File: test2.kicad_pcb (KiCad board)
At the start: 2 copper layers, 5 parts, among them Q1 IRLZ34N, U1 TEENSY3.1, U2 HCPL3120

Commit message: POC traco
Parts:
- added U3: TRACO_TEL_DCDC, DIP-24__600_ELL, F.Cu at (111.8, 88.9)
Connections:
- U1 pad 15: (no net) -> N-000009

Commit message: switched to version 4 of kicad...
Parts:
- Q1: footprint TO220 -> TO_SOT_Packages_THT:TO-220_Vertical
- R1: footprint R4 -> Resistors_THT:R_Axial_DIN0204_L3.6mm_D1.6mm_P5.08mm_Horizontal
- R2: footprint R3-LARGE_PADS -> Resistors_THT:R_Axial_DIN0204_L3.6mm_D1.6mm_P5.08mm_Horizontal
- U1: footprint DIP-28__600 -> Teensy:Teensy30_31_32_LC
- U2: footprint DIP-8__300 -> Housings_DIP:DIP-8_W7.62mm
- U3: footprint DIP-24__600_ELL -> Housings_DIP:DIP-24_W15.24mm
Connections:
- U1 pad 1: N-000008 -> Net-(U1-Pad1)
- U1 pad 10: (no net) -> Net-(U1-Pad10)
- U1 pad 11: (no net) -> Net-(U1-Pad11)
- U1 pad 12: (no net) -> Net-(U1-Pad12)
- U1 pad 13: (no net) -> Net-(U1-Pad13)
- U1 pad 14: (no net) -> Net-(U1-Pad14)
- U1 pad 15: N-000009 -> Net-(U1-Pad15)
- U1 pad 16: (no net) -> Net-(U1-Pad16)
- U1 pad 17: (no net) -> Net-(U1-Pad17)
- U1 pad 18: (no net) -> Net-(U1-Pad18)
- U1 pad 19: (no net) -> Net-(U1-Pad19)
- U1 pad 2: (no net) -> Net-(U1-Pad2)
- U1 pad 20: (no net) -> Net-(U1-Pad20)
- U1 pad 21: (no net) -> Net-(U1-Pad21)
- U1 pad 22: (no net) -> Net-(U1-Pad22)
- U1 pad 23: (no net) -> Net-(U1-Pad23)
- U1 pad 24: (no net) -> Net-(U1-Pad24)
- U1 pad 25: (no net) -> Net-(U1-Pad25)
- U1 pad 26: (no net) -> Net-(U1-Pad26)
- U1 pad 27: (no net) -> Net-(U1-Pad27)
- U1 pad 28: (no net) -> Net-(U1-Pad28)
- U1 pad 3: (no net) -> Net-(U1-Pad3)
- U1 pad 4: (no net) -> Net-(U1-Pad4)
- U1 pad 6: (no net) -> Net-(U1-Pad6)
- U1 pad 7: (no net) -> Net-(U1-Pad7)
- U1 pad 8: (no net) -> Net-(U1-Pad8)
- U1 pad 9: (no net) -> Net-(U1-Pad9)
- U2 pad 1: (no net) -> Net-(U2-Pad1)
- U2 pad 3: N-000008 -> Net-(U1-Pad1)
- U2 pad 4: (no net) -> Net-(U2-Pad4)
- U2 pad 6: (no net) -> Net-(U2-Pad6)
- U3 pad 1: (no net) -> Net-(U1-Pad15)
- U3 pad 10: (no net) -> +5V
- U3 pad 11: (no net) -> GND
- U3 pad 2: (no net) -> Net-(U1-Pad1)
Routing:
- net (no net): track 0.00 -> 182.4 mm
- net +5V: track 106.6 -> 0.00 mm
- net Net-(U1-Pad1): track 0.00 -> 59.7 mm
- net N-000008: track 59.7 -> 0.00 mm
- net Net-(Q1-Pad2): track 54.5 -> 0.00 mm
- net Net-(U1-Pad20): track 0.00 -> 44.3 mm
- net GND: track 38.9 -> 0.00 mm
- net Net-(Q1-Pad1): track 21.4 -> 38.9 mm

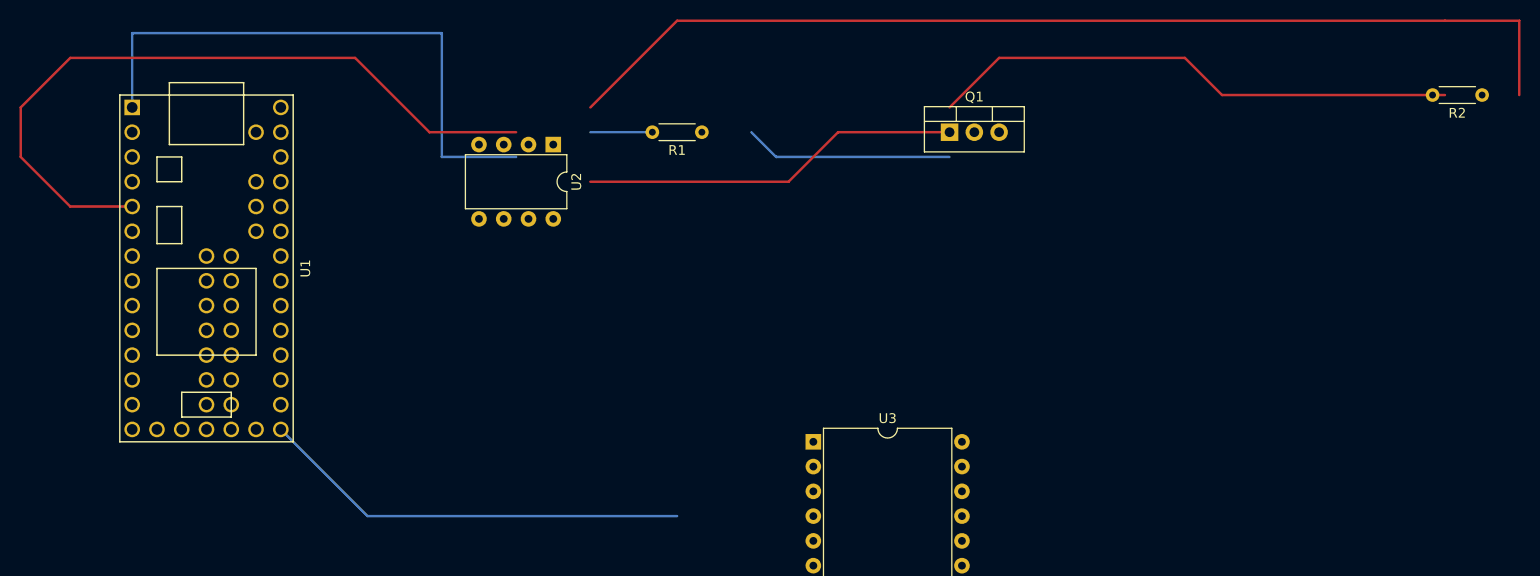
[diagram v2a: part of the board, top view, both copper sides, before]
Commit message: more messing araound to get kicad 4 happy
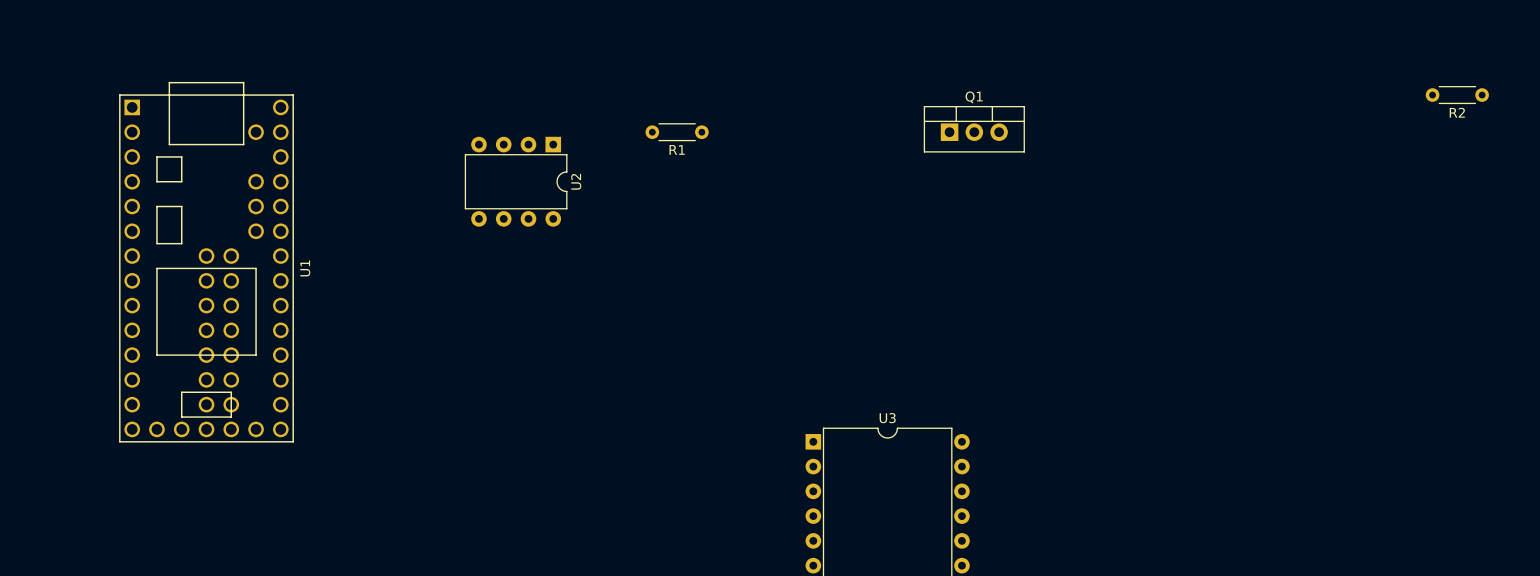
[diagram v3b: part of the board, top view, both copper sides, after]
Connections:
- U3 pad 1: Net-(U1-Pad15) -> +5V
- U3 pad 10: +5V -> Net-(U1-Pad33)
- U3 pad 11: GND -> Net-(U1-Pad1)
- U3 pad 12: (no net) -> GND
- U3 pad 2: Net-(U1-Pad1) -> (no net)
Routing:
- net (no net): track 182.4 -> 0.00 mm
- net Net-(U1-Pad5): track 74.7 -> 0.00 mm
- net Net-(U1-Pad1): track 59.7 -> 0.00 mm
- net Net-(U1-Pad20): track 44.3 -> 0.00 mm
- net Net-(Q1-Pad1): track 38.9 -> 0.00 mm
- net Net-(R1-Pad2): track 6.35 -> 0.00 mm
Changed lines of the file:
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@@
     (thickness 1.6)
     (drawings 0)
-    (tracks 27)
+    (tracks 0)
     (zones 0)
     (modules 6)
@@
     (fp_arc (start 7.62 -1.39) (end 6.62 -1.39) (angle -180) (layer F.SilkS) (width 0.12))
     (pad 1 thru_hole rect (at 0 0) (size 1.6 1.6) (drill 0.8) (layers *.Cu *.Mask)
-      (net 20 "Net-(U1-Pad15)"))
+      (net 1 +5V))
     (pad 13 thru_hole oval (at 15.24 27.94) (size 1.6 1.6) (drill 0.8) (layers *.Cu *.Mask))
-    (pad 2 thru_hole oval (at 0 2.54) (size 1.6 1.6) (drill 0.8) (layers *.Cu *.Mask)
-      (net 6 "Net-(U1-Pad1)"))
+    (pad 2 thru_hole oval (at 0 2.54) (size 1.6 1.6) (drill 0.8) (layers *.Cu *.Mask))
     (pad 14 thru_hole oval (at 15.24 25.4) (size 1.6 1.6) (drill 0.8) (layers *.Cu *.Mask))
     (pad 3 thru_hole oval (at 0 5.08) (size 1.6 1.6) (drill 0.8) (layers *.Cu *.Mask))
@@
     (pad 21 thru_hole oval (at 15.24 7.62) (size 1.6 1.6) (drill 0.8) (layers *.Cu *.Mask))
     (pad 10 thru_hole oval (at 0 22.86) (size 1.6 1.6) (drill 0.8) (layers *.Cu *.Mask)
-      (net 1 +5V))
+      (net 41 "Net-(U1-Pad33)"))
     (pad 22 thru_hole oval (at 15.24 5.08) (size 1.6 1.6) (drill 0.8) (layers *.Cu *.Mask))
     (pad 11 thru_hole oval (at 0 25.4) (size 1.6 1.6) (drill 0.8) (layers *.Cu *.Mask)
+      (net 6 "Net-(U1-Pad1)"))
+    (pad 23 thru_hole oval (at 15.24 2.54) (size 1.6 1.6) (drill 0.8) (layers *.Cu *.Mask))
+    (pad 12 thru_hole oval (at 0 27.94) (size 1.6 1.6) (drill 0.8) (layers *.Cu *.Mask)
       (net 2 GND))
-    (pad 23 thru_hole oval (at 15.24 2.54) (size 1.6 1.6) (drill 0.8) (layers *.Cu *.Mask))
-    (pad 12 thru_hole oval (at 0 27.94) (size 1.6 1.6) (drill 0.8) (layers *.Cu *.Mask))
     (pad 24 thru_hole oval (at 15.24 0) (size 1.6 1.6) (drill 0.8) (layers *.Cu *.Mask))
     (model Housings_DIP.3dshapes/DIP-24_W15.24mm.wrl
@@
     )
   )
-  (segment (start 176.53 45.72) (end 184.15 45.72) (width 0.254) (layer F.Cu) (net 0))
-  (segment (start 97.79 45.72) (end 176.53 45.72) (width 0.254) (layer F.Cu) (net 0))
-  (segment (start 88.9 54.61) (end 97.79 45.72) (width 0.254) (layer F.Cu) (net 0))
-  (segment (start 184.15 45.72) (end 184.15 53.34) (width 0.254) (layer F.Cu) (net 0))
-  (segment (start 125.73 59.69) (end 107.95 59.69) (width 0.254) (layer B.Cu) (net 0))
-  (segment (start 107.95 59.69) (end 105.41 57.15) (width 0.254) (layer B.Cu) (net 0))
-  (segment (start 176.53 53.34) (end 153.67 53.34) (width 0.254) (layer F.Cu) (net 0))
-  (segment (start 130.81 49.53) (end 125.73 54.61) (width 0.254) (layer F.Cu) (net 0))
-  (segment (start 149.86 49.53) (end 130.81 49.53) (width 0.254) (layer F.Cu) (net 0))
-  (segment (start 153.67 53.34) (end 149.86 49.53) (width 0.254) (layer F.Cu) (net 0))
-  (segment (start 125.73 57.15) (end 114.3 57.15) (width 0.254) (layer F.Cu) (net 3))
-  (segment (start 109.22 62.23) (end 88.9 62.23) (width 0.254) (layer F.Cu) (net 3))
-  (segment (start 114.3 57.15) (end 109.22 62.23) (width 0.254) (layer F.Cu) (net 3))
-  (segment (start 95.25 57.15) (end 88.9 57.15) (width 0.254) (layer B.Cu) (net 5))
-  (segment (start 41.91 54.61) (end 41.91 46.99) (width 0.254) (layer B.Cu) (net 6))
-  (segment (start 73.66 59.69) (end 81.28 59.69) (width 0.254) (layer B.Cu) (net 6))
-  (segment (start 73.66 46.99) (end 73.66 59.69) (width 0.254) (layer B.Cu) (net 6))
-  (segment (start 41.91 46.99) (end 73.66 46.99) (width 0.254) (layer B.Cu) (net 6))
-  (segment (start 41.91 64.77) (end 35.56 64.77) (width 0.254) (layer F.Cu) (net 10))
-  (segment (start 72.39 57.15) (end 81.28 57.15) (width 0.254) (layer F.Cu) (net 10))
-  (segment (start 64.77 49.53) (end 72.39 57.15) (width 0.254) (layer F.Cu) (net 10))
-  (segment (start 35.56 49.53) (end 64.77 49.53) (width 0.254) (layer F.Cu) (net 10))
-  (segment (start 30.48 54.61) (end 35.56 49.53) (width 0.254) (layer F.Cu) (net 10))
-  (segment (start 30.48 59.69) (end 30.48 54.61) (width 0.254) (layer F.Cu) (net 10))
-  (segment (start 35.56 64.77) (end 30.48 59.69) (width 0.254) (layer F.Cu) (net 10))
-  (segment (start 97.79 96.52) (end 66.04 96.52) (width 0.254) (layer B.Cu) (net 25))
-  (segment (start 66.04 96.52) (end 57.15 87.63) (width 0.254) (layer B.Cu) (net 25))
 )

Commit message: i feel like i am making a little progress again
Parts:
- added Q2: IRLZ34N, TO_SOT_Packages_THT:TO-220_Horizontal_Reversed, F.Cu at (108.0, 20.3)
- added Q3: IRLZ34N, TO_SOT_Packages_THT:TO-220_Horizontal, F.Cu at (101.6, -8.89)
- added R3: R, Resistors_THT:R_Axial_DIN0204_L3.6mm_D1.6mm_P5.08mm_Horizontal, F.Cu at (100.3, 74.9)
- added R4: R, Resistors_THT:R_Axial_DIN0204_L3.6mm_D1.6mm_P5.08mm_Horizontal, F.Cu at (118.1, 78.7)
- added R5: R, Resistors_THT:R_Axial_DIN0204_L3.6mm_D1.6mm_P5.08mm_Horizontal, F.Cu at (100.3, 99.1)
- added R6: R, Resistors_THT:R_Axial_DIN0204_L3.6mm_D1.6mm_P5.08mm_Horizontal, F.Cu at (134.6, 81.3)
- added U4: HCPL3120, Housings_DIP:DIP-8_W7.62mm, F.Cu at (78.7, 74.9)
- added U5: HCPL3120, Housings_DIP:DIP-8_W7.62mm, F.Cu at (80.0, 92.7)
- moved U3 74.5 mm to (58.4, 141.0), turned to 90 degrees

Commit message: thats a full loay out :) only 3 channels and lots of bits missing but it shows the idea
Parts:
- Q1: footprint TO_SOT_Packages_THT:TO-220_Vertical -> TO_SOT_Packages_THT:TO-220_Horizontal
- Q2: footprint TO_SOT_Packages_THT:TO-220_Horizontal_Reversed -> TO_SOT_Packages_THT:TO-220_Horizontal
- moved R5 83.9 mm to (180.3, 73.7), turned to 180 degrees
- moved Q3 72.4 mm to (120.7, 61.0), turned to 270 degrees
- moved Q2 58.5 mm to (120.7, 77.5), turned to 270 degrees
- moved R6 51.7 mm to (180.3, 57.1), turned to 180 degrees
- moved Q1 37.2 mm to (120.7, 94.0), turned to 270 degrees
- moved R1 36.9 mm to (97.8, 94.0)
- moved R2 36.8 mm to (180.3, 90.2)
- moved U5 34.3 mm to (78.7, 58.4)
- moved U2 33.6 mm to (78.7, 91.4), turned to 0 degrees
- moved R4 27.0 mm to (97.8, 61.0), turned to 180 degrees
- moved R3 3.59 mm to (97.8, 77.5), turned to 180 degrees
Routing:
- net +5V: track 0.00 -> 267.6 mm
- net GND: track 0.00 -> 193.0 mm
- net Net-(U1-Pad1): track 0.00 -> 188.8 mm
- net Net-(U1-Pad33): track 0.00 -> 125.2 mm
- net Net-(U1-Pad7): track 0.00 -> 119.9 mm
- net Net-(U1-Pad6): track 0.00 -> 116.1 mm
- net Net-(U1-Pad5): track 0.00 -> 112.2 mm
- net Net-(Q2-Pad2): track 0.00 -> 57.2 mm
- net Net-(Q3-Pad2): track 0.00 -> 57.2 mm
- net Net-(Q1-Pad2): track 0.00 -> 57.2 mm
- net Net-(Q3-Pad1): track 0.00 -> 22.9 mm
- net Net-(Q2-Pad1): track 0.00 -> 22.9 mm
- net Net-(Q1-Pad1): track 0.00 -> 22.9 mm
- net Net-(R4-Pad2): track 0.00 -> 10.2 mm
- net Net-(R3-Pad2): track 0.00 -> 10.2 mm
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
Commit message: 8 chanels, not finished
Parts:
- added D1: D, Diodes_THT:D_5KP_P10.16mm_Horizontal, F.Cu at (132.1, 96.5)
- added D2: D, Diodes_THT:D_5KP_P10.16mm_Horizontal, F.Cu at (132.1, 81.3)
- added D3: D, Diodes_THT:D_5KP_P10.16mm_Horizontal, F.Cu at (133.3, 63.5)
- added D4: D, Diodes_THT:D_5KP_P10.16mm_Horizontal, F.Cu at (133.3, 109.2)
- added D5: D, Diodes_THT:D_5KP_P10.16mm_Horizontal, F.Cu at (132.1, 123.2)
- added D6: D, Diodes_THT:D_5KP_P10.16mm_Horizontal, F.Cu at (129.5, 141.0)
- added D7: D, Diodes_THT:D_5KP_P10.16mm_Horizontal, F.Cu at (129.5, 158.8)
- added D8: D, Diodes_THT:D_5KP_P10.16mm_Horizontal, F.Cu at (129.5, 175.3)
- added Q4: IRLZ34N, TO_SOT_Packages_THT:TO-220_Vertical, F.Cu at (120.7, 108.0)
- added Q5: IRLZ34N, TO_SOT_Packages_THT:TO-220_Vertical, F.Cu at (120.7, 123.2)
- added Q6: IRLZ34N, TO_SOT_Packages_THT:TO-220_Vertical, F.Cu at (118.1, 141.0)
- added Q7: IRLZ34N, TO_SOT_Packages_THT:TO-220_Vertical, F.Cu at (118.1, 156.2)
- added Q8: IRLZ34N, TO_SOT_Packages_THT:TO-220_Vertical, F.Cu at (118.1, 174.0)
- added R10: R, Diodes_THT:D_5W_P5.08mm_Vertical_AnodeUp, F.Cu at (154.9, 80.0)
- added R11: R, Diodes_THT:D_5W_P5.08mm_Vertical_AnodeUp, F.Cu at (154.9, 63.5)
- added R12: R, Diodes_THT:D_5W_P5.08mm_Vertical_AnodeUp, F.Cu at (154.9, 111.8)
- added R13: R, Diodes_THT:D_5W_P5.08mm_Vertical_AnodeUp, F.Cu at (156.2, 124.5)
- added R14: R, Diodes_THT:D_5W_P5.08mm_Vertical_AnodeUp, F.Cu at (156.2, 141.0)
- added R15: R, Diodes_THT:D_5W_P5.08mm_Vertical_AnodeUp, F.Cu at (156.2, 158.8)
- added R16: R, Diodes_THT:D_5W_P5.08mm_Vertical_AnodeUp, F.Cu at (157.5, 175.3)
- added R7: R, Diodes_THT:D_5KP_P10.16mm_Horizontal, F.Cu at (105.4, 125.7)
- added R8: R, Diodes_THT:D_5KP_P10.16mm_Horizontal, F.Cu at (106.7, 141.0)
- added R9: R, Diodes_THT:D_5W_P5.08mm_Vertical_AnodeUp, F.Cu at (156.2, 99.1)
- added U10: HCPL3120, Housings_DIP:DIP-8_W7.62mm, F.Cu at (78.7, 171.4)
- added U6: HCPL3120, Housings_DIP:DIP-8_W7.62mm, F.Cu at (78.7, 108.0)
- added U7: HCPL3120, Housings_DIP:DIP-8_W7.62mm, F.Cu at (78.7, 123.2)
- added U8: HCPL3120, Housings_DIP:DIP-8_W7.62mm, F.Cu at (78.7, 138.4)
- added U9: HCPL3120, Housings_DIP:DIP-8_W7.62mm, F.Cu at (78.7, 153.7)
- Q1, Q2, Q3: footprint TO_SOT_Packages_THT:TO-220_Horizontal -> TO_SOT_Packages_THT:TO-220_Vertical
- R1, R2, R3, R4, R5, R6: footprint Resistors_THT:R_Axial_DIN0204_L3.6mm_D1.6mm_P5.08mm_Horizontal -> Diodes_THT:D_5KP_P10.16mm_Horizontal
- moved R5 129.0 mm to (104.1, 177.8)
- moved R4 96.8 mm to (105.4, 157.5)
- moved R6 92.0 mm to (105.4, 110.5)
- moved R2 79.4 mm to (101.6, 80.0)
- moved U3 26.2 mm to (35.6, 128.3)
- moved R3 19.3 mm to (105.4, 59.7)
- moved R1 7.62 mm to (105.4, 94.0)
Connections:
- net Net-(U1-Pad5) renamed /Sheet58E8F73D/chanel1
- net Net-(U1-Pad6) renamed /Sheet58E8F73D/chanel2
- net Net-(U1-Pad7) renamed /Sheet58E8F73D/chanel3
- Q1 pad 2: Net-(Q1-Pad2) -> Net-(D1-Pad2)
- Q2 pad 2: Net-(Q2-Pad2) -> Net-(D2-Pad2)
- Q3 pad 2: Net-(Q3-Pad2) -> Net-(D3-Pad2)
- R2 pad 1: +5V -> Net-(Q2-Pad1)
- R2 pad 2: Net-(Q1-Pad2) -> Net-(R2-Pad2)
- R3 pad 1: Net-(Q2-Pad1) -> Net-(Q3-Pad1)
- R4 pad 1: Net-(Q3-Pad1) -> Net-(Q7-Pad1)
- R5 pad 1: +5V -> Net-(Q8-Pad1)
- R5 pad 2: Net-(Q2-Pad2) -> Net-(R5-Pad2)
- R6 pad 1: +5V -> Net-(Q4-Pad1)
- R6 pad 2: Net-(Q3-Pad2) -> Net-(R6-Pad2)
- U1 pad 1: Net-(U1-Pad1) -> /Sheet58E8F73D/cleanGND
- U1 pad 10: Net-(U1-Pad10) -> (no net)
- U1 pad 11: Net-(U1-Pad11) -> (no net)
- U1 pad 12: Net-(U1-Pad12) -> (no net)
- U1 pad 13: Net-(U1-Pad13) -> (no net)
- U1 pad 14: Net-(U1-Pad14) -> (no net)
- U1 pad 15: Net-(U1-Pad15) -> (no net)
- U1 pad 16: Net-(U1-Pad16) -> (no net)
- U1 pad 17: Net-(U1-Pad17) -> (no net)
- U1 pad 18: Net-(U1-Pad18) -> (no net)
- U1 pad 19: Net-(U1-Pad19) -> (no net)
- U1 pad 2: Net-(U1-Pad2) -> (no net)
- U1 pad 20: Net-(U1-Pad20) -> (no net)
- U1 pad 21: Net-(U1-Pad21) -> (no net)
- U1 pad 22: Net-(U1-Pad22) -> (no net)
- U1 pad 23: Net-(U1-Pad23) -> (no net)
- U1 pad 24: Net-(U1-Pad24) -> (no net)
- U1 pad 25: Net-(U1-Pad25) -> (no net)
- U1 pad 26: Net-(U1-Pad26) -> (no net)
- U1 pad 27: Net-(U1-Pad27) -> /Sheet58E8F73D/chanel8
- U1 pad 28: Net-(U1-Pad28) -> /Sheet58E8F73D/chanel7
- U1 pad 29: Net-(U1-Pad29) -> /Sheet58E8F73D/chanel6
- U1 pad 3: Net-(U1-Pad3) -> (no net)
- U1 pad 30: Net-(U1-Pad30) -> /Sheet58E8F73D/changel5
- U1 pad 31: Net-(U1-Pad31) -> (no net)
- U1 pad 32: Net-(U1-Pad32) -> (no net)
- U1 pad 34: Net-(U1-Pad34) -> (no net)
- U1 pad 35: Net-(U1-Pad35) -> (no net)
- U1 pad 36: Net-(U1-Pad36) -> (no net)
- U1 pad 37: Net-(U1-Pad37) -> (no net)
- U1 pad 38: Net-(U1-Pad38) -> (no net)
- U1 pad 39: Net-(U1-Pad39) -> (no net)
- U1 pad 4: Net-(U1-Pad4) -> (no net)
- U1 pad 40: Net-(U1-Pad40) -> (no net)
- U1 pad 41: Net-(U1-Pad41) -> (no net)
- U1 pad 42: Net-(U1-Pad42) -> (no net)
- U1 pad 43: Net-(U1-Pad43) -> (no net)
- U1 pad 44: Net-(U1-Pad44) -> (no net)
- U1 pad 45: Net-(U1-Pad45) -> (no net)
- U1 pad 46: Net-(U1-Pad46) -> (no net)
- U1 pad 47: Net-(U1-Pad47) -> (no net)
- U1 pad 48: Net-(U1-Pad48) -> (no net)
- U1 pad 49: Net-(U1-Pad49) -> (no net)
- U1 pad 50: Net-(U1-Pad50) -> (no net)
- U1 pad 51: Net-(U1-Pad51) -> (no net)
- U1 pad 8: Net-(U1-Pad8) -> /Sheet58E8F73D/chanel4
- U1 pad 9: Net-(U1-Pad9) -> (no net)
- U2 pad 1: Net-(U2-Pad1) -> (no net)
- U2 pad 3: Net-(U1-Pad1) -> /Sheet58E8F73D/cleanGND
- U2 pad 4: Net-(U2-Pad4) -> (no net)
- U2 pad 6: Net-(U2-Pad6) -> (no net)
- U2 pad 8: +5V -> +24V
- U3 pad 1: +5V -> Net-(U1-Pad33)
- U3 pad 10: Net-(U1-Pad33) -> +24V
- U3 pad 11: Net-(U1-Pad1) -> GND
- U3 pad 12: GND -> /Sheet58E8F73D/cleanGND
- U4 pad 1: Net-(U4-Pad1) -> (no net)
- U4 pad 3: Net-(U1-Pad1) -> /Sheet58E8F73D/cleanGND
- U4 pad 4: Net-(U4-Pad4) -> (no net)
- U4 pad 6: Net-(U4-Pad6) -> (no net)
- U4 pad 7: Net-(R3-Pad2) -> Net-(R2-Pad2)
- U4 pad 8: +5V -> +24V
- U5 pad 1: Net-(U5-Pad1) -> (no net)
- U5 pad 3: Net-(U1-Pad1) -> /Sheet58E8F73D/cleanGND
- U5 pad 4: Net-(U5-Pad4) -> (no net)
- U5 pad 6: Net-(U5-Pad6) -> (no net)
- U5 pad 7: Net-(R4-Pad2) -> Net-(R3-Pad2)
- U5 pad 8: +5V -> +24V
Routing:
- net +5V: track 267.6 -> 0.00 mm
- net (no net): track 0.00 -> 249.4 mm
- net Net-(U1-Pad1): track 188.8 -> 0.00 mm
- net /Sheet58E8F73D/cleanGND: track 0.00 -> 188.8 mm
- net +24V: track 0.00 -> 140.1 mm
- net Net-(Q2-Pad2): track 57.2 -> 0.00 mm
- net Net-(Q3-Pad2): track 57.2 -> 0.00 mm
- net Net-(Q1-Pad2): track 57.2 -> 0.00 mm
- net Net-(R8-Pad2): track 0.00 -> 41.9 mm
- net GND: track 193.0 -> 151.1 mm
- net Net-(D2-Pad2): track 0.00 -> 16.6 mm
- net Net-(D3-Pad2): track 0.00 -> 16.6 mm
- net Net-(D1-Pad2): track 0.00 -> 16.6 mm
- net Net-(R4-Pad2): track 10.2 -> 0.00 mm
- net Net-(R2-Pad2): track 0.00 -> 10.2 mm
